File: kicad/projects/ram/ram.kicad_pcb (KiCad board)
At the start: 2 copper layers, 203.2 x 97.8 mm, 6 parts, among them J1 peripheral_addr_bus_connector, J2 peripheral_aux_connector, J3 peripheral_membank_connector

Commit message: RAM schematic 80 percent complete and initial layout of PCB.
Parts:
- added C1: 20pF, Capacitor_THT:C_Disc_D5.0mm_W2.5mm_P5.00mm, F.Cu at (357.0, 78.2)
- added C10: C, Capacitor_THT:C_Disc_D5.0mm_W2.5mm_P5.00mm, F.Cu at (365.1, 86.3)
- added C11: C, Capacitor_THT:C_Disc_D5.0mm_W2.5mm_P5.00mm, F.Cu at (365.1, 90.4)
- added C12: C, Capacitor_THT:C_Disc_D5.0mm_W2.5mm_P5.00mm, F.Cu at (365.1, 94.4)
- added C13: C, Capacitor_THT:C_Disc_D5.0mm_W2.5mm_P5.00mm, F.Cu at (365.1, 98.5)
- added C2: 0pF, Capacitor_THT:C_Disc_D5.0mm_W2.5mm_P5.00mm, F.Cu at (357.0, 82.3)
- added C3: C, Capacitor_THT:C_Disc_D5.0mm_W2.5mm_P5.00mm, F.Cu at (357.0, 86.3)
- added C4: C, Capacitor_THT:C_Disc_D5.0mm_W2.5mm_P5.00mm, F.Cu at (357.0, 90.4)
- added C5: C, Capacitor_THT:C_Disc_D5.0mm_W2.5mm_P5.00mm, F.Cu at (357.0, 94.4)
- added C6: C, Capacitor_THT:C_Disc_D5.0mm_W2.5mm_P5.00mm, F.Cu at (357.0, 98.5)
- added C7: C, Capacitor_THT:C_Disc_D5.0mm_W2.5mm_P5.00mm, F.Cu at (357.0, 102.5)
- added C8: C, Capacitor_THT:C_Disc_D5.0mm_W2.5mm_P5.00mm, F.Cu at (365.1, 78.2)
- added C9: C, Capacitor_THT:C_Disc_D5.0mm_W2.5mm_P5.00mm, F.Cu at (365.1, 82.3)
- added J5: Conn_02x16_Odd_Even, Connector_PinHeader_2.54mm:PinHeader_2x16_P2.54mm_Vertical, F.Cu at (101.6, 134.6)
- added R1: 4.7K, Resistor_THT:R_Axial_DIN0207_L6.3mm_D2.5mm_P10.16mm_Horizontal, F.Cu at (343.0, 120.6)
- added R2: 4.7K, Resistor_THT:R_Axial_DIN0207_L6.3mm_D2.5mm_P10.16mm_Horizontal, F.Cu at (343.0, 124.6)
- added RN1: R_Network08_US, Resistor_THT:R_Array_SIP9, F.Cu at (99.1, 127.0)
- added RN2: R_Network08_US, Resistor_THT:R_Array_SIP9, F.Cu at (142.2, 121.9)
- added U1: 74HC02, Package_DIP:DIP-14_W7.62mm_Socket, F.Cu at (74.9, 68.6)
- added U10: 74HC30, Package_DIP:DIP-14_W7.62mm_Socket, F.Cu at (124.5, 114.3)
- added U11: 74HC32, Package_DIP:DIP-14_W7.62mm_Socket, F.Cu at (99.1, 99.1)
- added U12: 74HC08, Package_DIP:DIP-14_W7.62mm_Socket, F.Cu at (124.5, 99.1)
- added U2: 74HC08, Package_DIP:DIP-14_W7.62mm_Socket, F.Cu at (99.1, 68.6)
- added U3: 74HC123, Package_DIP:DIP-16_W7.62mm_Socket, F.Cu at (121.9, 68.6)
- added U4: 74HC04, Package_DIP:DIP-14_W7.62mm_Socket, F.Cu at (147.3, 68.6)
- added U5: 74HC245, Package_DIP:DIP-20_W7.62mm_Socket, F.Cu at (223.5, 121.9)
- added U6: 74HC245, Package_DIP:DIP-20_W7.62mm_Socket, F.Cu at (203.2, 135.9)
- added U7: 628128_DIP32_SSOP32, Package_DIP:DIP-32_W15.24mm_Socket, F.Cu at (228.6, 66.0)
- added U8: 628128_DIP32_SSOP32, Package_DIP:DIP-32_W15.24mm_Socket, F.Cu at (185.4, 68.6)
- added U9: 74HC30, Package_DIP:DIP-14_W7.62mm_Socket, F.Cu at (99.1, 114.3)
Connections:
- J2 pad 10: unconnected-(J2-RFM-Pad10) -> /RFM
- J2 pad 12: unconnected-(J2-WTM-Pad12) -> /WTM
- J2 pad 14: unconnected-(J2-RST-Pad14) -> /RESET
- J2 pad 6: unconnected-(J2-DCLK-Pad6) -> /DATA_CLK
- J2 pad 8: unconnected-(J2-CCLK-Pad8) -> /CTL_CLK

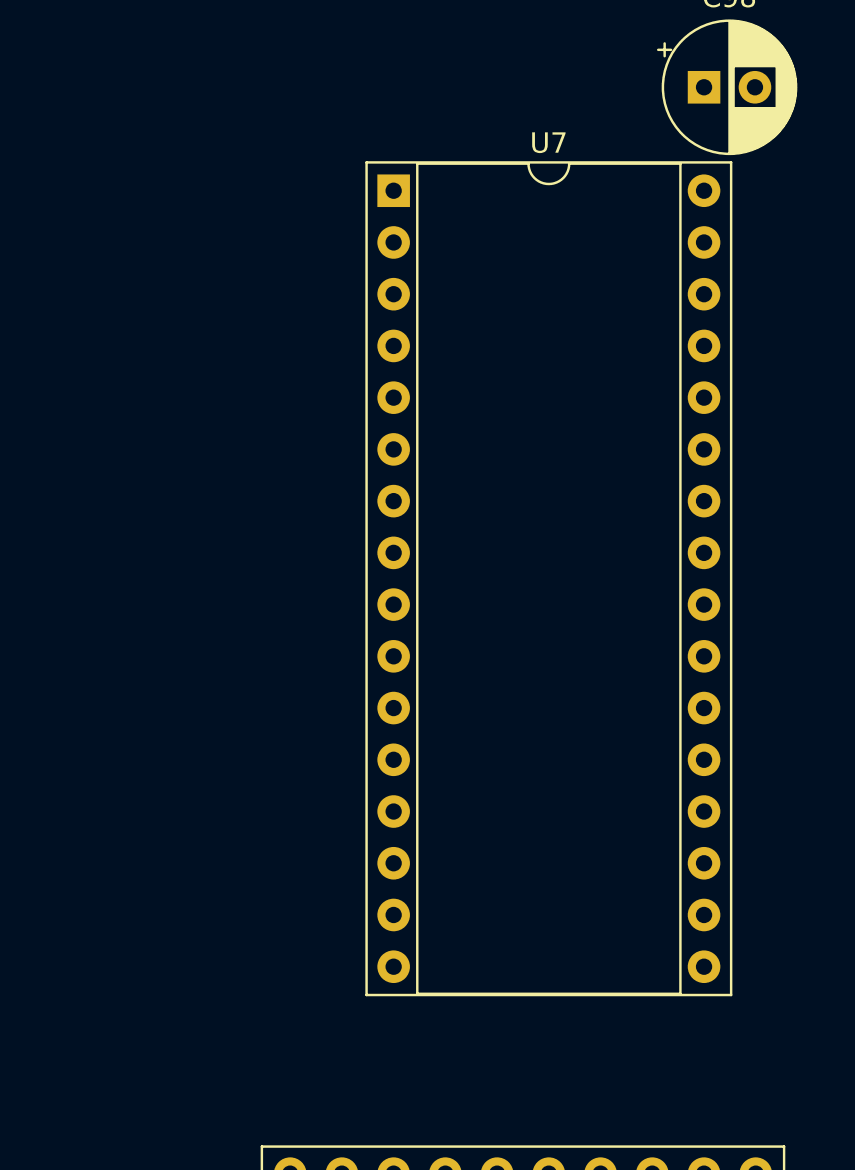
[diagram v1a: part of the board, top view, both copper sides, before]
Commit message: Clean up some ERC checks in RAM
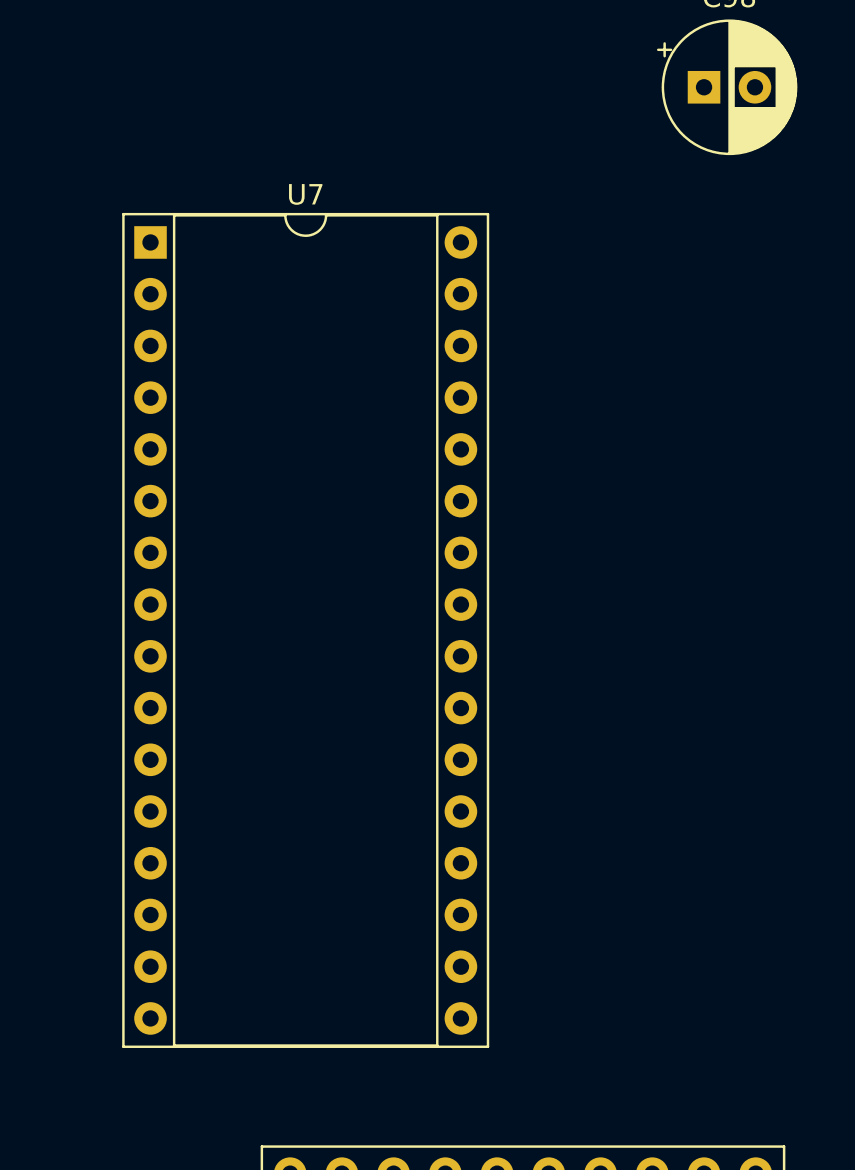
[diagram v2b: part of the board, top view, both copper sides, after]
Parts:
- moved U7 12.2 mm to (216.7, 68.6)
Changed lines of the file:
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@@
   )
   (footprint "Package_DIP:DIP-32_W15.24mm_Socket" (layer "F.Cu")
-    (at 228.6 66.04)
+    (at 216.662 68.58)
     (descr "32-lead though-hole mounted DIP package, row spacing 15.24 mm (600 mils), Socket")
     (tags "THT DIP DIL PDIP 2.54mm 15.24mm 600mil Socket")

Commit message: Start laying out RAM wiring.
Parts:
- added TP1: TestPoint, Connector_PinHeader_2.54mm:PinHeader_1x01_P2.54mm_Vertical, F.Cu at (154.4, 23.6)
- added TP2: TestPoint, Connector_PinHeader_2.54mm:PinHeader_1x01_P2.54mm_Vertical, F.Cu at (152.9, 35.1)
- added TP3: TestPoint, Connector_PinHeader_2.54mm:PinHeader_1x01_P2.54mm_Vertical, F.Cu at (142.7, 35.1)
- added TP4: TestPoint, Connector_PinHeader_2.54mm:PinHeader_1x01_P2.54mm_Vertical, F.Cu at (168.9, 37.8)
- moved C3 174.3 mm to (185.4, 116.8), turned to -90 degrees
- moved C4 141.1 mm to (218.4, 116.8), turned to -90 degrees
- moved C1 32.9 mm to (332.8, 55.9)
- moved C2 28.8 mm to (345.4, 55.9)
- moved U6 17.1 mm to (190.5, 124.5)
- moved U7 14.5 mm to (231.1, 68.6)
- moved U8 12.7 mm to (198.1, 68.6)
- moved RN1 3.59 mm to (96.5, 124.5)
- moved RN2 3.59 mm to (144.8, 124.5)
- moved U5 2.54 mm to (223.5, 124.5)
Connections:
- C10 pad 1: unconnected-(C10-Pad1) -> VCC
- C10 pad 2: unconnected-(C10-Pad2) -> GND
- C11 pad 1: unconnected-(C11-Pad1) -> VCC
- C11 pad 2: unconnected-(C11-Pad2) -> GND
- C12 pad 1: unconnected-(C12-Pad1) -> VCC
- C12 pad 2: unconnected-(C12-Pad2) -> GND
- C13 pad 1: unconnected-(C13-Pad1) -> VCC
- C13 pad 2: unconnected-(C13-Pad2) -> GND
- C3 pad 1: unconnected-(C3-Pad1) -> VCC
- C3 pad 2: unconnected-(C3-Pad2) -> GND
- C4 pad 1: unconnected-(C4-Pad1) -> VCC
- C4 pad 2: unconnected-(C4-Pad2) -> GND
- C5 pad 1: unconnected-(C5-Pad1) -> VCC
- C5 pad 2: unconnected-(C5-Pad2) -> GND
- C6 pad 1: unconnected-(C6-Pad1) -> VCC
- C6 pad 2: unconnected-(C6-Pad2) -> GND
- U1 pad 14: unconnected-(U1E-VCC-Pad14) -> VCC
- U1 pad 7: unconnected-(U1E-GND-Pad7) -> GND
- U10 pad 14: unconnected-(U10B-VCC-Pad14) -> VCC
- U10 pad 7: unconnected-(U10B-GND-Pad7) -> GND
- U11 pad 10: unconnected-(U11-Pad10) -> GND
- U11 pad 12: unconnected-(U11-Pad12) -> GND
- U11 pad 13: unconnected-(U11-Pad13) -> GND
- U11 pad 14: unconnected-(U11E-VCC-Pad14) -> VCC
- U11 pad 4: unconnected-(U11-Pad4) -> GND
- U11 pad 5: unconnected-(U11-Pad5) -> GND
- U11 pad 7: unconnected-(U11E-GND-Pad7) -> GND
- U11 pad 9: unconnected-(U11-Pad9) -> GND
- U12 pad 10: unconnected-(U12-Pad10) -> GND
- U12 pad 12: unconnected-(U12-Pad12) -> GND
- U12 pad 13: unconnected-(U12-Pad13) -> GND
- U12 pad 14: unconnected-(U12E-VCC-Pad14) -> VCC
- U12 pad 7: unconnected-(U12E-GND-Pad7) -> GND
- U12 pad 9: unconnected-(U12-Pad9) -> GND
- U2 pad 14: unconnected-(U2E-VCC-Pad14) -> VCC
- U2 pad 4: unconnected-(U2-Pad4) -> GND
- U2 pad 5: unconnected-(U2-Pad5) -> GND
- U2 pad 7: unconnected-(U2E-GND-Pad7) -> GND
- U3 pad 16: unconnected-(U3C-VCC-Pad16) -> VCC
- U3 pad 8: unconnected-(U3C-GND-Pad8) -> GND
- U4 pad 1: unconnected-(U4-Pad1) -> GND
- U4 pad 14: unconnected-(U4G-VCC-Pad14) -> VCC
- U4 pad 3: unconnected-(U4-Pad3) -> GND
- U4 pad 5: unconnected-(U4-Pad5) -> GND
- U4 pad 7: unconnected-(U4G-GND-Pad7) -> GND
- U4 pad 9: unconnected-(U4-Pad9) -> GND
- U9 pad 14: unconnected-(U9B-VCC-Pad14) -> VCC
- U9 pad 7: unconnected-(U9B-GND-Pad7) -> GND
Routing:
- net /ADDR_BUS_15: track 0.00 -> 144.7 mm
- net /ADDR_BUS_13: track 0.00 -> 138.7 mm, vias 0 -> 4
- net /ADDR_BUS_11: track 0.00 -> 132.7 mm, vias 0 -> 2
- net /ADDR_BUS_09: track 0.00 -> 131.2 mm, vias 0 -> 2
- net /ADDR_BUS_08: track 0.00 -> 130.9 mm, vias 0 -> 2
- net /ADDR_BUS_10: track 0.00 -> 129.2 mm, vias 0 -> 2
- net /ADDR_BUS_14: track 0.00 -> 126.8 mm
- net /ADDR_BUS_12: track 0.00 -> 123.0 mm
- net /ADDR_BUS_07: track 0.00 -> 115.5 mm
- net /ADDR_BUS_06: track 0.00 -> 113.1 mm
- net /ADDR_BUS_05: track 0.00 -> 110.8 mm
- net /ADDR_BUS_04: track 0.00 -> 108.5 mm
- net /ADDR_BUS_03: track 0.00 -> 106.2 mm
- net /ADDR_BUS_01: track 0.00 -> 101.5 mm
- net /ADDR_BUS_00: track 0.00 -> 99.2 mm
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
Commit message: First pass of RAM PCB complete
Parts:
- added C14: C, Capacitor_THT:C_Disc_D5.0mm_W2.5mm_P5.00mm, F.Cu at (241.4, 61.7)
- added D1: LED, sixteen-bit-computer:LED_D5.0mm_Horizontal_O3.81mm_Z3.0mm, F.Cu at (61.0, 63.5)
- added R3: 1K, Resistor_THT:R_Axial_DIN0207_L6.3mm_D2.5mm_P10.16mm_Horizontal, F.Cu at (58.4, 68.6)
- added TP5: GND, Connector_Pin:Pin_D1.0mm_L10.0mm, F.Cu at (195.3, 61.5)
- added TP6: Data Clk, Connector_Pin:Pin_D1.0mm_L10.0mm, F.Cu at (143.5, 61.5)
- RN1, RN2: value R_Network08_US -> 10K
- TP1: value TestPoint -> Long Pulse / RAM ~{WE}; footprint Connector_PinHeader_2.54mm:PinHeader_1x01_P2.54mm_Vertical -> Connector_Pin:Pin_D1.0mm_L10.0mm
- TP2: value TestPoint -> Data Buf Dir; footprint Connector_PinHeader_2.54mm:PinHeader_1x01_P2.54mm_Vertical -> Connector_Pin:Pin_D1.0mm_L10.0mm
- TP3: value TestPoint -> Data Buf ~{OE}; footprint Connector_PinHeader_2.54mm:PinHeader_1x01_P2.54mm_Vertical -> Connector_Pin:Pin_D1.0mm_L10.0mm
- TP4: value TestPoint -> Short Pulse; footprint Connector_PinHeader_2.54mm:PinHeader_1x01_P2.54mm_Vertical -> Connector_Pin:Pin_D1.0mm_L10.0mm
- moved C8 309.3 mm to (55.9, 78.7), turned to 90 degrees
- moved C5 301.1 mm to (55.9, 96.5), turned to -90 degrees
- moved C9 283.9 mm to (81.3, 78.7), turned to 90 degrees
- moved C6 275.7 mm to (81.3, 96.5), turned to -90 degrees
- moved R1 268.7 mm to (81.3, 59.7)
- moved C10 256.2 mm to (109.2, 73.7), turned to -90 degrees
- moved C12 255.9 mm to (109.2, 96.5), turned to -90 degrees
- moved C2 248.0 mm to (97.8, 68.6), turned to 90 degrees
- moved R2 243.9 mm to (108.0, 59.7), turned to 180 degrees
- moved C1 241.7 mm to (91.4, 68.6), turned to 90 degrees
- moved C11 231.1 mm to (134.6, 73.7), turned to -90 degrees
- moved C13 230.5 mm to (134.6, 96.5), turned to -90 degrees
- moved C97 170.0 mm to (221.0, 110.5)
- moved C7 154.1 mm to (208.4, 61.7)
- moved U4 70.6 mm to (86.4, 104.1)
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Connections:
- net /RW_BUF_DIR renamed /DATA_BUF_DIR
- net /RW_BUF_~{OE} renamed /DATA_BUF_~{OE}
- U11 pad 4: GND -> Net-(U11-Pad3)
- U11 pad 5: GND -> Net-(U11-Pad3)
- U11 pad 6: unconnected-(U11-Pad6) -> Net-(R3-Pad2)
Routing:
- net VCC: track 0.00 -> 668.4 mm, vias 0 -> 20
- net /DATA_BUF_DIR: track 0.00 -> 230.7 mm, vias 0 -> 5
- net /DATA_CLK: track 0.00 -> 220.7 mm, vias 0 -> 6
- net /DATA_BUF_~{OE}: track 0.00 -> 218.5 mm, vias 0 -> 6
- net /RAM_~{WE}: track 0.00 -> 179.2 mm, vias 0 -> 5
- net /RFM: track 0.00 -> 171.8 mm, vias 0 -> 2
- net /WTM: track 0.00 -> 162.0 mm, vias 0 -> 2
- net Net-(U3B-~{Q}): track 0.00 -> 104.8 mm, vias 0 -> 2
- net /ADDRESSED_WTM: track 0.00 -> 97.0 mm, vias 0 -> 3
- net Net-(R3-Pad2): track 0.00 -> 77.2 mm, vias 0 -> 2
- net /SAFE_CLK: track 0.00 -> 70.3 mm, vias 0 -> 2
- net /ADDRESSED_RFM: track 0.00 -> 68.6 mm, vias 0 -> 3
- net Net-(U10A-~{Y}): track 0.00 -> 50.7 mm, vias 0 -> 2
- net Net-(U3A-Q): track 0.00 -> 44.1 mm
- net Net-(J5-Pin_16): track 0.00 -> 39.9 mm, vias 0 -> 2
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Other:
- board text added: "ADDRESS IN ENABLED BANK"
- board text added: "BANK ENABLE (JUMPER ON = ENABLE)"
- board text added: "JLCJLCJLCJLC"
- board text added: "RAM"
- board text added: "v 1.0"

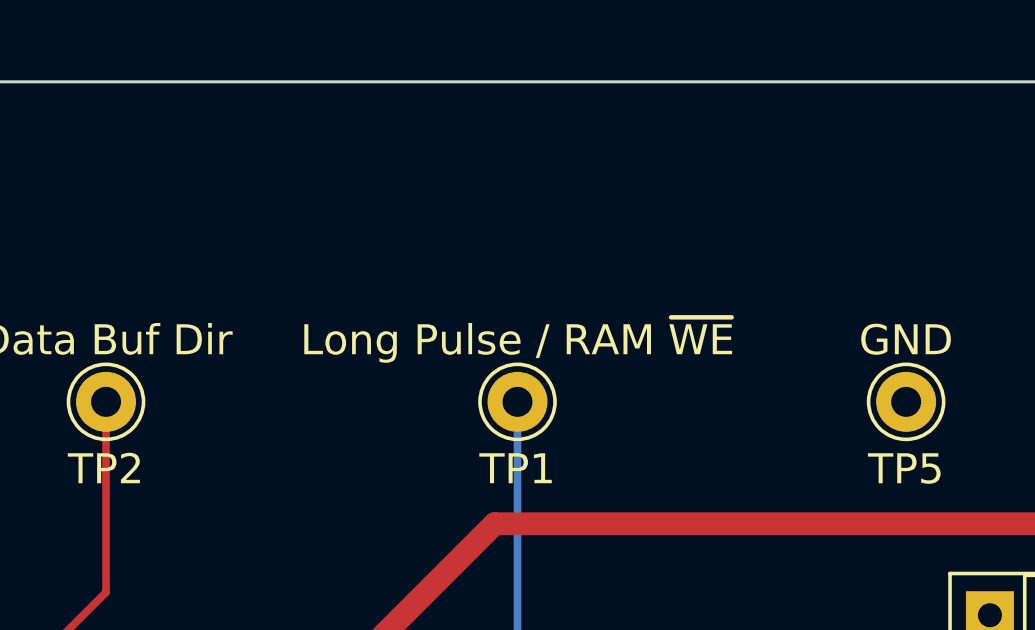
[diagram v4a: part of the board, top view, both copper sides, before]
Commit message: Updates design rules and constraints in peripheral boards. Make a start on CPU board template.
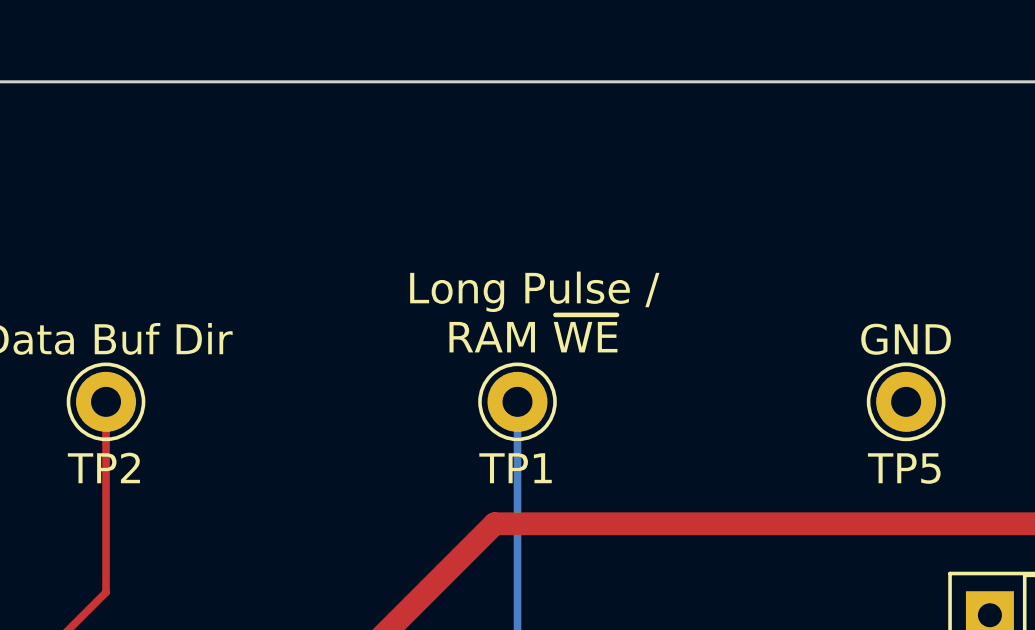
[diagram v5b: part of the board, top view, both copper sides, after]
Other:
- board text added: "Long Pulse / RAM ~{WE}"
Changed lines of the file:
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@@
         (effects (font (size 1 1) (thickness 0.15)))
     )
-    (fp_text value "Long Pulse / RAM ~{WE}" (at 0 -2.05) (layer "F.SilkS")
+    (fp_text value "Long Pulse / RAM ~{WE}" (at 0.254 3.81) (layer "F.Fab")
         (effects (font (size 1 1) (thickness 0.15)))
     )
@@
     (effects (font (size 1.27 1.27) (thickness 0.2032)) (justify bottom))
   )
+  (gr_text "Long Pulse /\nRAM ~{WE}" (at 182.88 59.944) (layer "F.SilkS")
+    (effects (font (size 1.016 1.016) (thickness 0.1524)) (justify bottom))
+  )
   (gr_text "BANK ENABLE\n(JUMPER ON = ENABLE)" (at 103.378 125.222) (layer "F.SilkS")
